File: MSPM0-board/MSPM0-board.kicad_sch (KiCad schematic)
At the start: 0 parts

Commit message: mspm0(feat): add sheet data
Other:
- company: (none) -> Slemanz
- title: (none) -> MSPM0 Board
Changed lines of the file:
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@@
 	(generator_version "9.0")
 	(paper "A4")
+	(title_block
+		(title "MSPM0 Board")
+		(date "2026-01-09")
+		(rev "A")
+		(company "Slemanz")
+	)
 	(sheet_instances
 		(path "/"

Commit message: mspm0(feat): begin schematic
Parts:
- added C1: 10u, Capacitor_SMD:C_0805_2012Metric, symbol Device:C
- added C2: 470n, Capacitor_SMD:C_0603_1608Metric, symbol Device:C
- added U1: MSPM0G3507SPTR, Package_QFP:LQFP-48_7x7mm_P0.5mm, symbol symbol_lib:MSPM0G3507SPTR

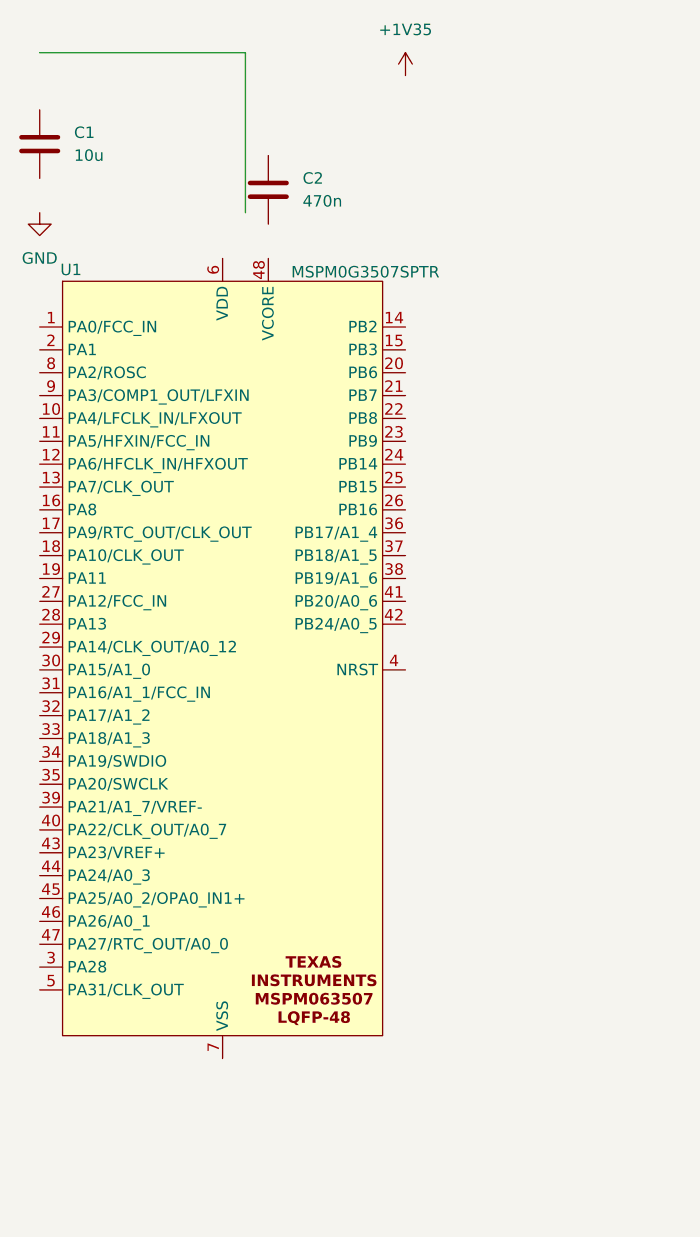
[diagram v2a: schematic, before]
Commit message: mspm0(feat): add mcu to schematic
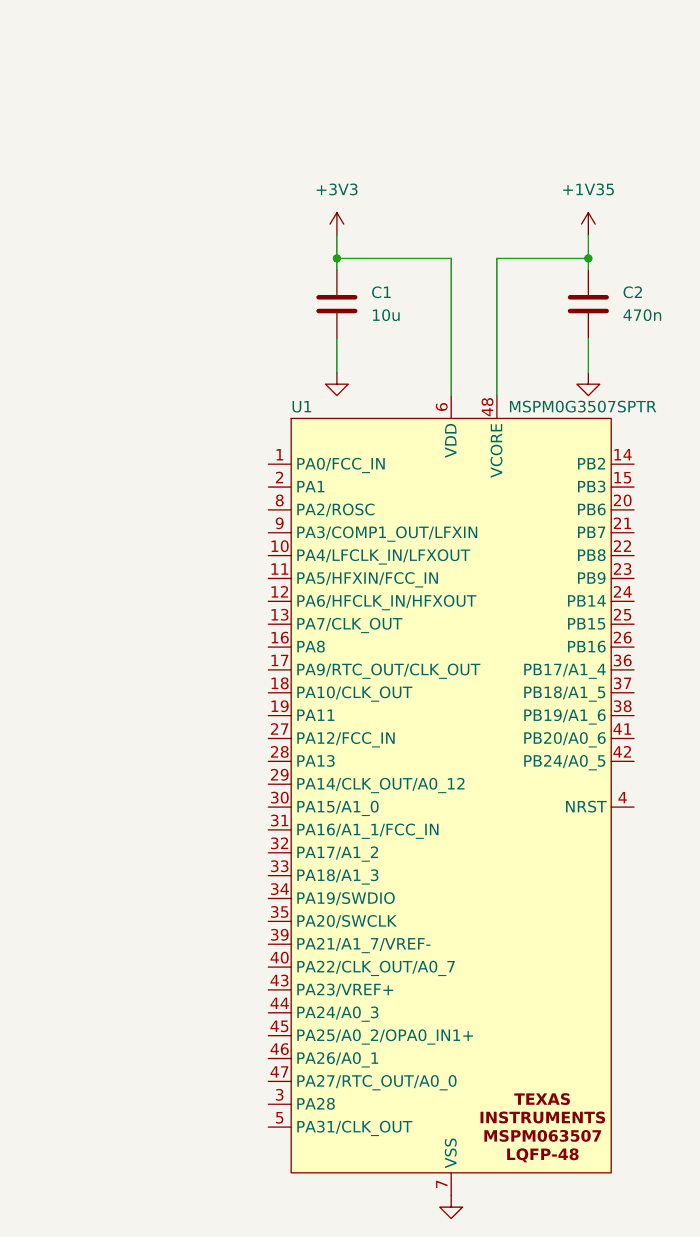
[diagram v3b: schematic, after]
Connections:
- net +1V35: now also C2.1, U1.48 (VCORE)
- net GND: now also C1.2, C2.2, U1.7 (VSS)
- net +3V3: now reaches U1.6 (VDD)
- net +3V3: now also C1.1
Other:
- moved on the sheet: C1, C2

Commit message: mspm0(feat): add vref circuit
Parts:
- added C3: 470n, Capacitor_SMD:C_0603_1608Metric, symbol Device:C
- added R1: 0R, Resistor_SMD:R_0603_1608Metric, symbol Device:R
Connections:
- net GND: now also R1.2
- net VREF-: now reaches U1.39 (PA21/A1_7/VREF-)
- net VREF-: now also C3.1, R1.1
- net VREF+: now reaches U1.43 (PA23/VREF+)
- net VREF+: now also C3.2

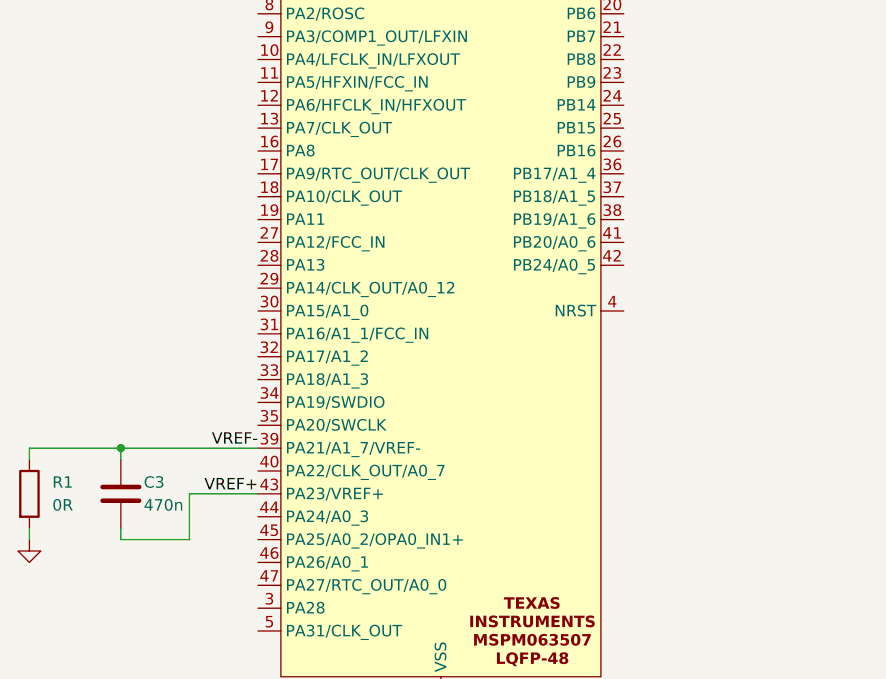
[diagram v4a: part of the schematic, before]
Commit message: mspm0(feat): add pull up to nrst
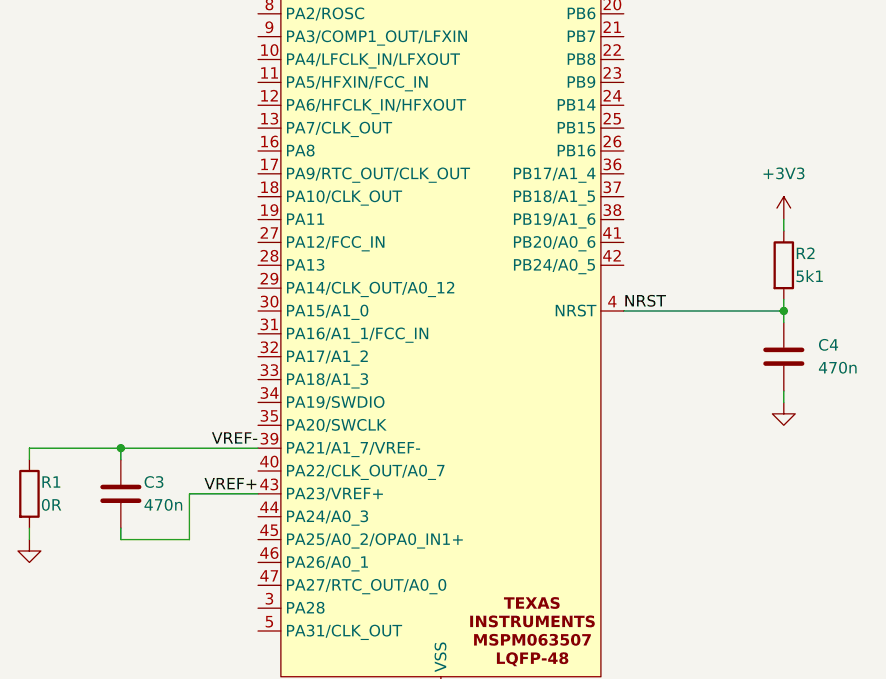
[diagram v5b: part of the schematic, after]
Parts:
- added C4: 470n, Capacitor_SMD:C_0603_1608Metric, symbol Device:C
- added R2: 5k1, Resistor_SMD:R_0603_1608Metric, symbol Device:R
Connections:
- net +3V3: now also R2.1
- net GND: now also C4.2
- net NRST: now reaches U1.4 (NRST)
- net NRST: now also C4.1, R2.2

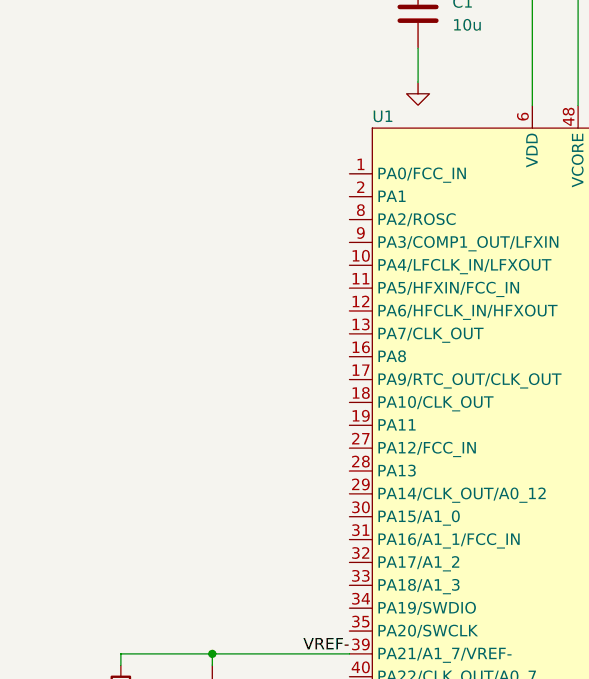
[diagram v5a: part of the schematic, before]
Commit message: mspm0(feat): add crystal
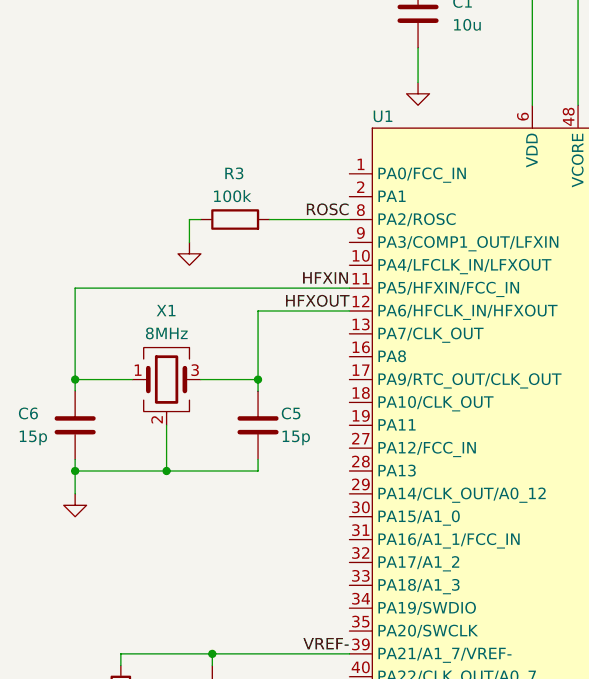
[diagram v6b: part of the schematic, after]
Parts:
- added C5, C6: 15p, Capacitor_SMD:C_0603_1608Metric, symbol Device:C
- added R3: 100k, Resistor_SMD:R_0603_1608Metric, symbol Device:R
- added X1: 8MHz, Crystal:Crystal_SMD_3225-4Pin_3.2x2.5mm, symbol Device:Crystal_GND24
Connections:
- net GND: now also C5.2, C6.2, R3.1, X1.2 (G), X1.4 (G)
- net HFXIN: now reaches U1.11 (PA5/HFXIN/FCC_IN)
- net HFXIN: now also C6.1, X1.1
- net HFXOUT: now reaches U1.12 (PA6/HFCLK_IN/HFXOUT)
- net HFXOUT: now also C5.1, X1.3
- net ROSC: now reaches U1.8 (PA2/ROSC)
- net ROSC: now also R3.2

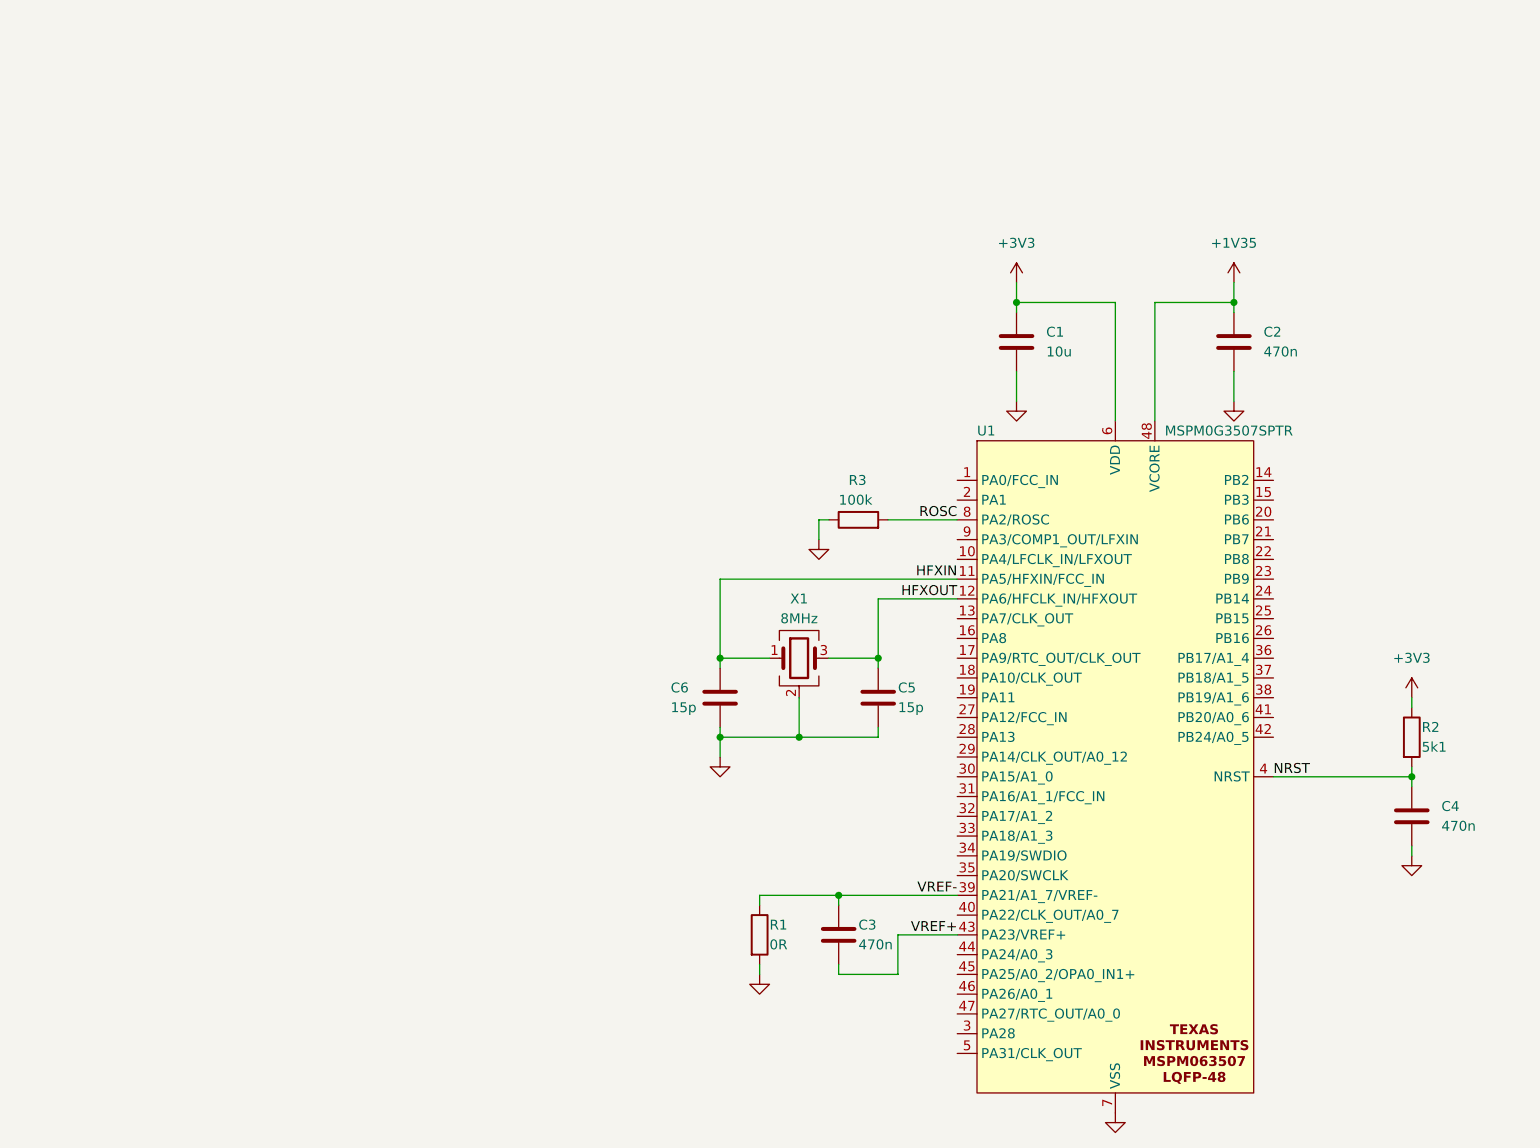
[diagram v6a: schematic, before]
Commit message: mspm0(feat): change usb symbol
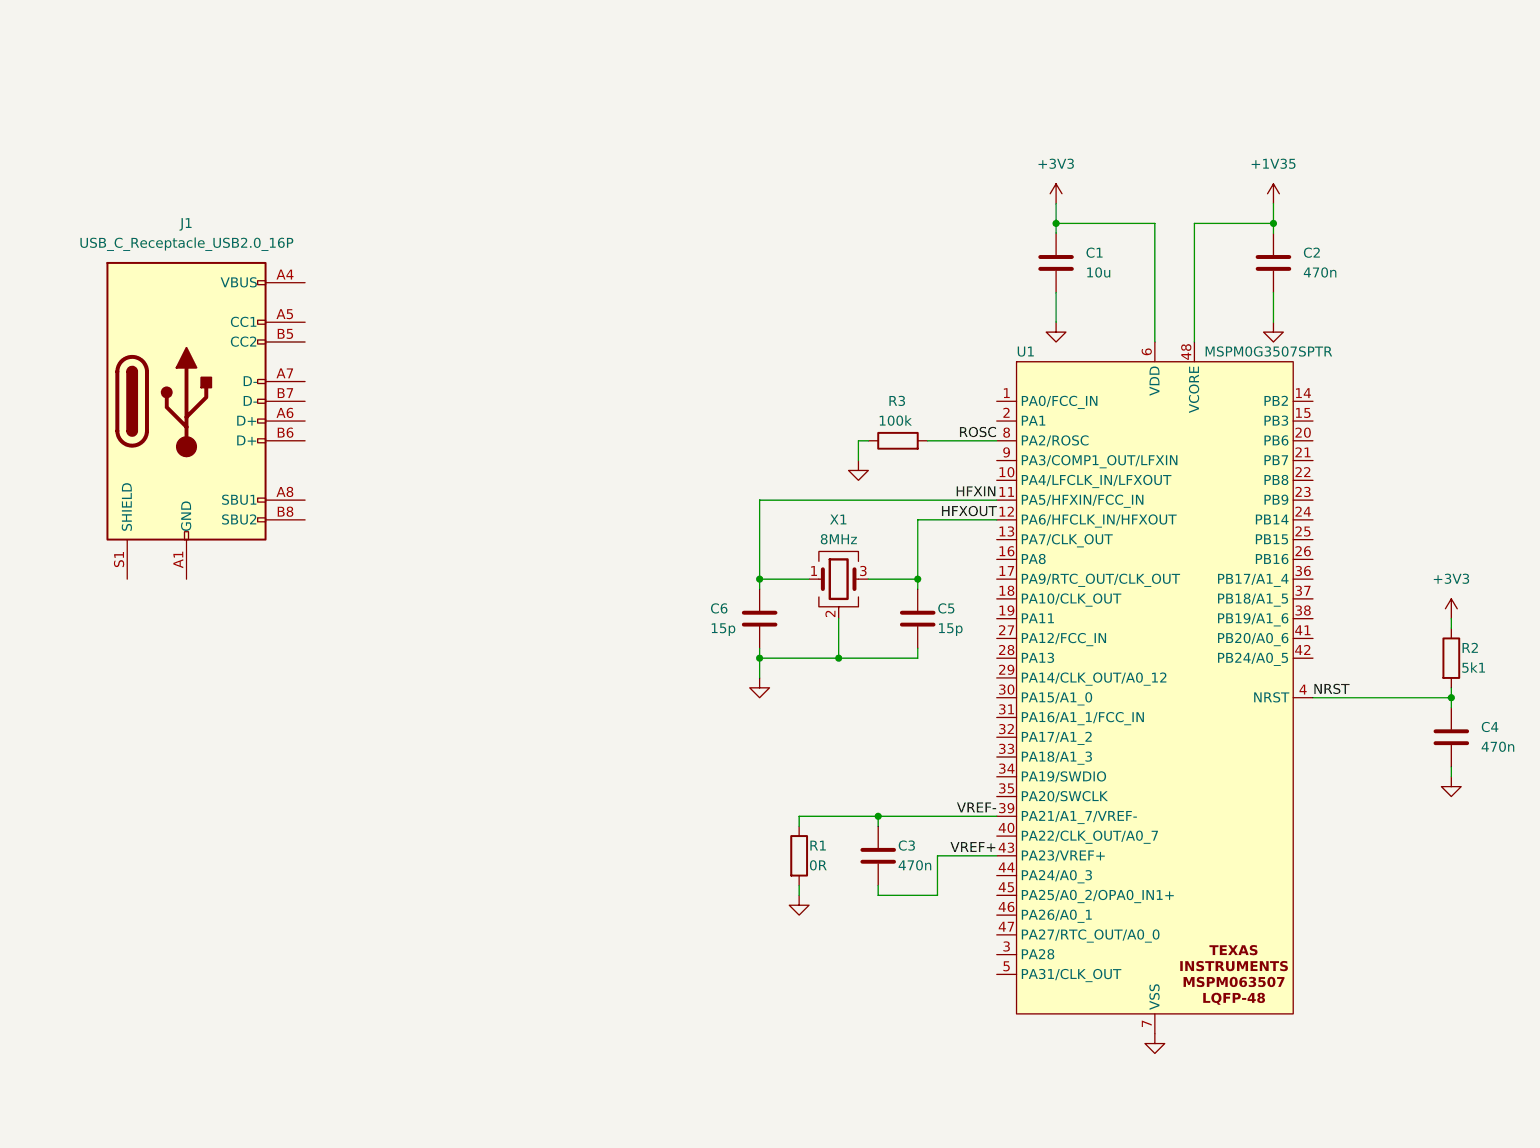
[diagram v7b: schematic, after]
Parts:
- added J1: USB_C_Receptacle_USB2.0_16P, symbol Connector:USB_C_Receptacle_USB2.0_16P
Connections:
- new net: J1.A1 (GND), J1.A12 (GND), J1.B1 (GND), J1.B12 (GND)
- new net: J1.A4 (VBUS), J1.A9 (VBUS), J1.B4 (VBUS), J1.B9 (VBUS)
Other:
- moved on the sheet: C1, C2, C3, C4, C5, C6, R1, R2, R3, U1, X1

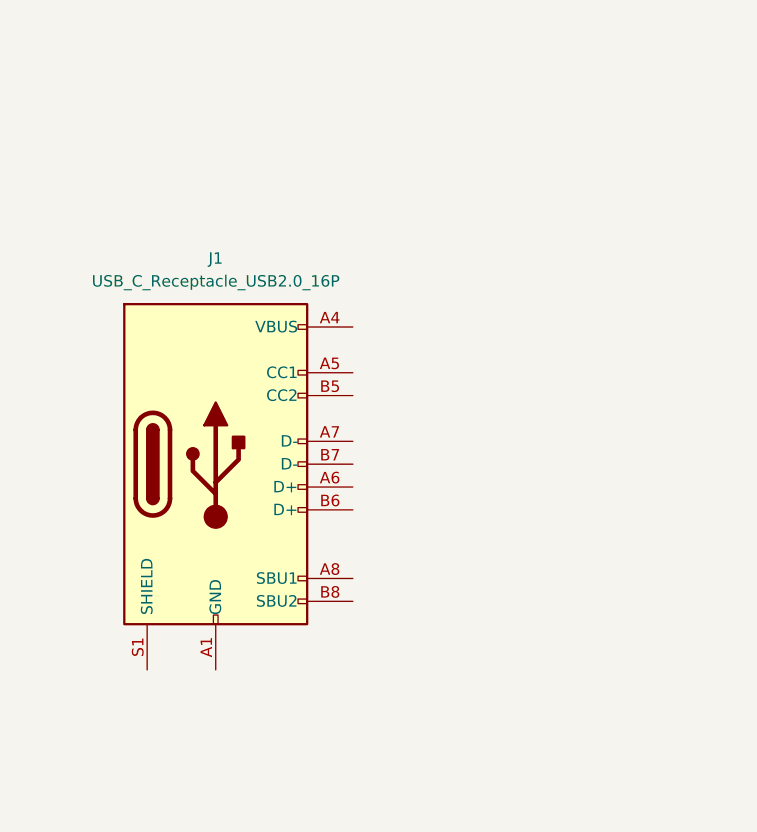
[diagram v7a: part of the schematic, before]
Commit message: mspm0(feat): add esd protection
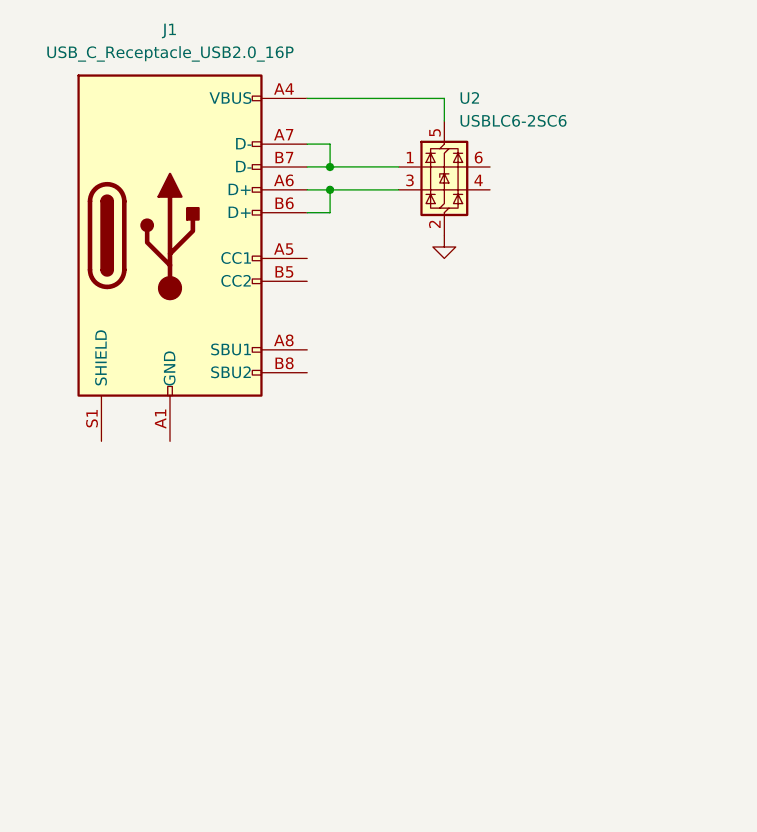
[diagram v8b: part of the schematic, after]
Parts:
- added U2: USBLC6-2SC6, Package_TO_SOT_SMD:SOT-23-6, symbol Power_Protection:USBLC6-2SC6
- J1: footprint (none) -> Connector_USB:USB_C_Receptacle_GCT_USB4105-xx-A_16P_TopMnt_Horizontal
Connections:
- net GND: now also U2.2 (GND)
- net at J1.A4 (VBUS), J1.A9 (VBUS), J1.B4 (VBUS)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: now also U2.5 (VBUS)
- net at J1.A6 (D+): now also J1.B6 (D+), U2.3 (I/O2)
- net at J1.A7 (D-): now also J1.B7 (D-), U2.1 (I/O1)
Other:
- moved on the sheet: J1
